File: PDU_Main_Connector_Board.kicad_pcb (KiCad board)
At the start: 2 copper layers, 48.3 x 64.8 mm, 3 parts, among them J1 776228-1, J2 Conn_02x02_Odd_Even

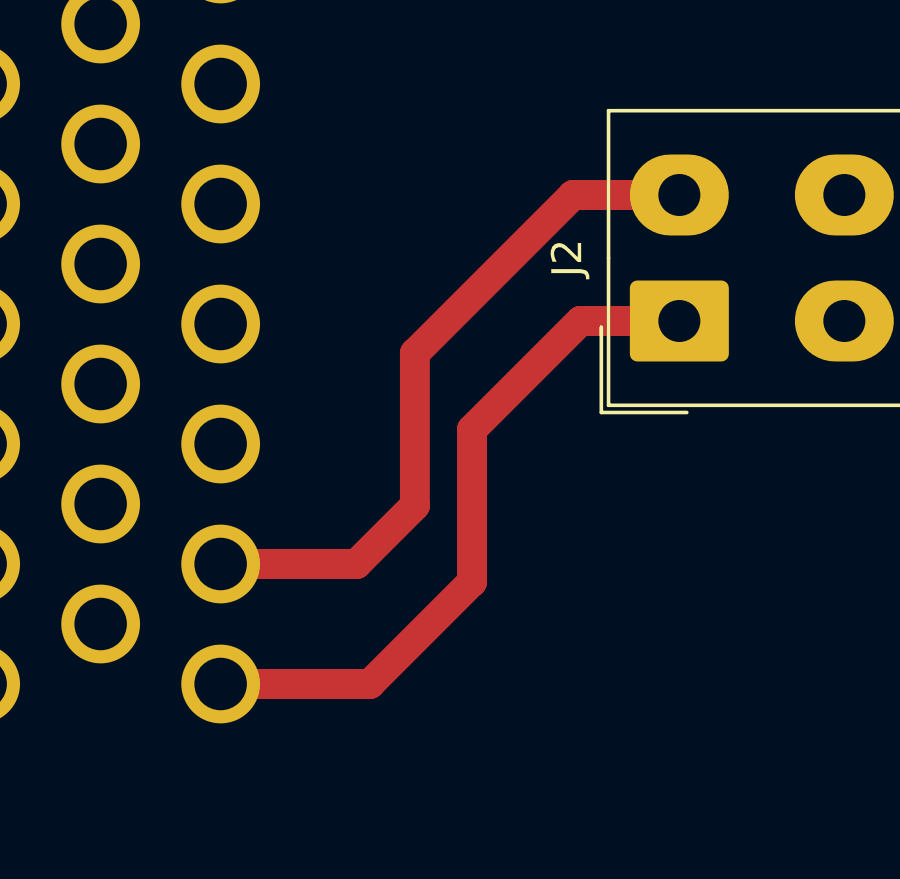
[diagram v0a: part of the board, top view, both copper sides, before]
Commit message: VER1.0: добавил схему по госту в доки, добавил дублирование CAN, добавил новые герберы
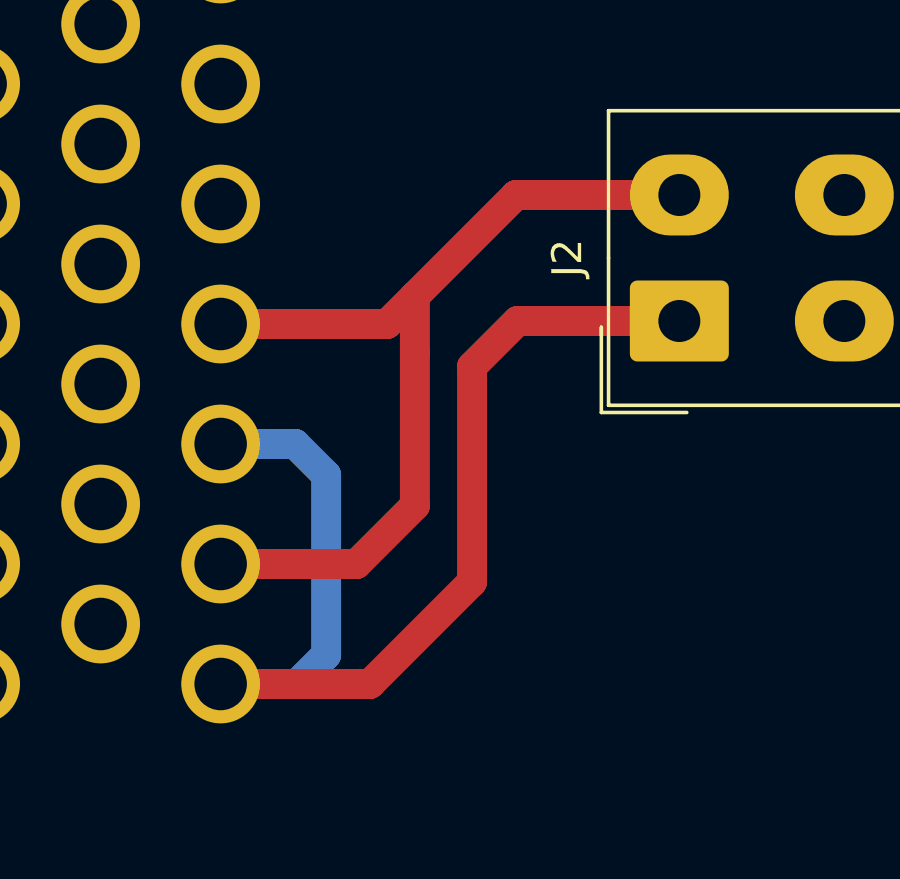
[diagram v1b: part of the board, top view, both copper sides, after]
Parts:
- J1: value 776228-1 -> ~
- J2: value Conn_02x02_Odd_Even -> ~
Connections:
- J1 pad 20: unconnected-(J1-Pad20) -> CANH
- J1 pad 21: unconnected-(J1-Pad21) -> CANL
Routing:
- net CANL: track 23.3 -> 38.4 mm
- net CANH: track 23.4 -> 31.3 mm
